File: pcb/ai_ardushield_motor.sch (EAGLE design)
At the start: 41 parts, among them IC1 PCA9685, IC2 TB6612FNG, IC3 TB6612FNG, J1 1X02ST, J10 1X04, J12 1X02ST, J2 1X03, J3 1X03, J4 1X06, J5 1X08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

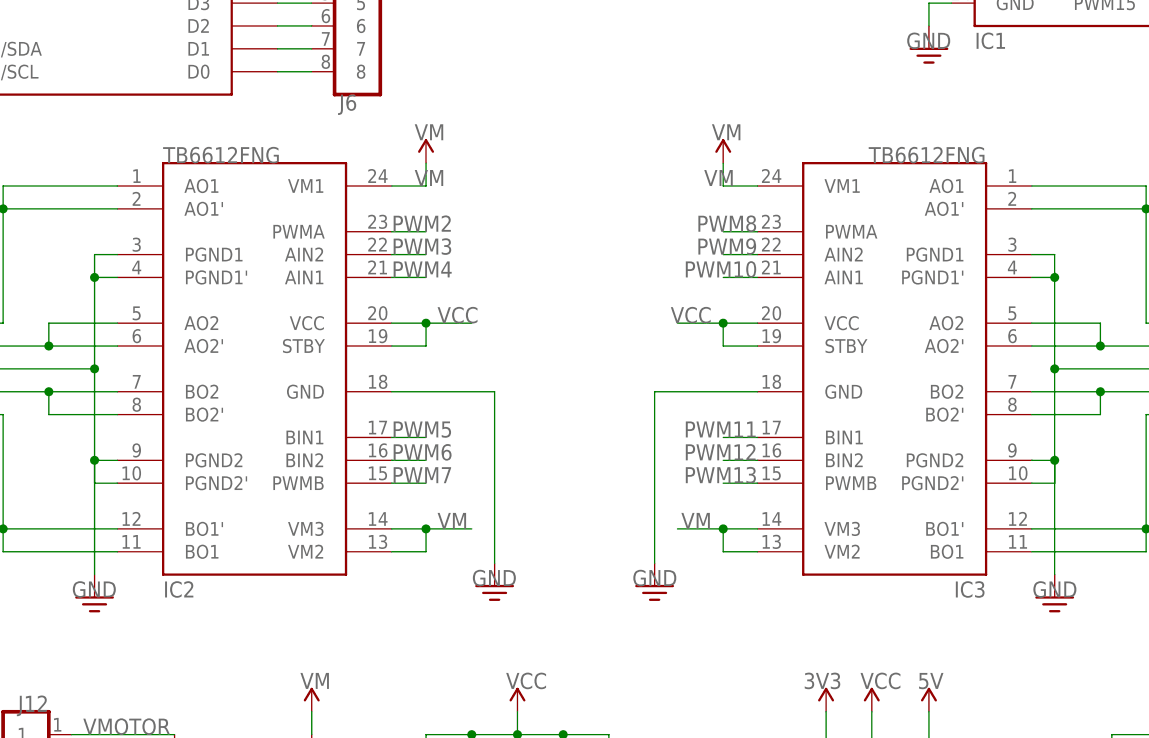
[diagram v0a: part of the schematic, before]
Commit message: Fixed a few minor warnings in the ERC.
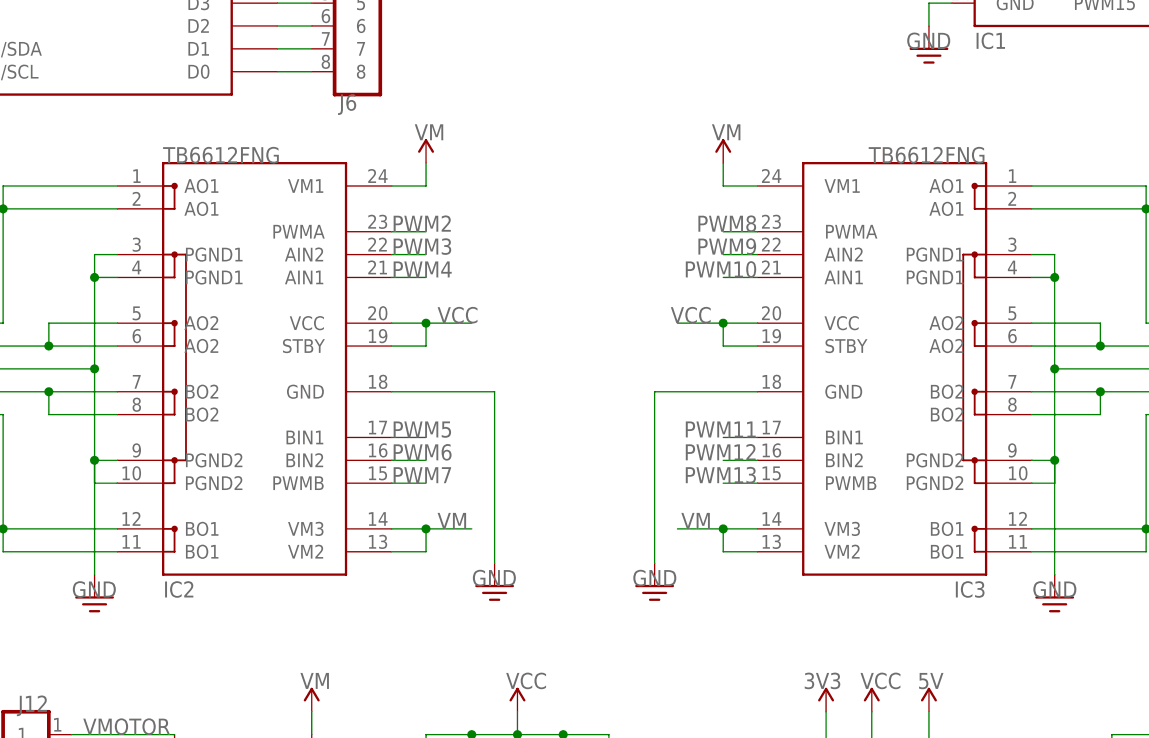
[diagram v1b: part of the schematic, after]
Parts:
- JS1, JS2, JS3, JS4, JS5: value (none) -> 1X02-SJNO
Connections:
- net GND: now also IC2.PGND1@1, IC2.PGND1@2, IC2.PGND2@1, IC2.PGND2@2, IC3.PGND1@1, IC3.PGND1@2, IC3.PGND2@1, IC3.PGND2@2; no longer IC2.PGND1, IC2.PGND1', IC2.PGND2, IC2.PGND2', IC3.PGND1, IC3.PGND1', IC3.PGND2, IC3.PGND2'
- net N$23: now also IC2.AO1@1, IC2.AO1@2; no longer IC2.AO1, IC2.AO1'
- net N$24: now also IC2.AO2@1, IC2.AO2@2; no longer IC2.AO2, IC2.AO2'
- net N$35: now also IC2.BO2@1, IC2.BO2@2; no longer IC2.BO2, IC2.BO2'
- net N$36: now also IC2.BO1@1, IC2.BO1@2; no longer IC2.BO1, IC2.BO1'
- net N$38: now also IC3.AO1@1, IC3.AO1@2; no longer IC3.AO1, IC3.AO1'
- net N$39: now also IC3.AO2@1, IC3.AO2@2; no longer IC3.AO2, IC3.AO2'
- net N$40: now also IC3.BO2@1, IC3.BO2@2; no longer IC3.BO2, IC3.BO2'
- net N$41: now also IC3.BO1@1, IC3.BO1@2; no longer IC3.BO1, IC3.BO1'
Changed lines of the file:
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@@
 <net name="N$23" class="1">
 <segment>
-<pinref part="IC2" gate="G$1" pin="AO1"/>
+<pinref part="IC2" gate="G$1" pin="AO1@1"/>
 <wire x1="77.47" y1="107.95" x2="64.77" y2="107.95" width="0.1524" layer="91"/>
 <wire x1="64.77" y1="107.95" x2="64.77" y2="105.41" width="0.1524" layer="91"/>
 <wire x1="64.77" y1="105.41" x2="64.77" y2="92.71" width="0.1524" layer="91"/>
 <wire x1="64.77" y1="92.71" x2="60.96" y2="92.71" width="0.1524" layer="91"/>
-<pinref part="IC2" gate="G$1" pin="AO1'"/>
+<pinref part="IC2" gate="G$1" pin="AO1@2"/>
 <wire x1="77.47" y1="105.41" x2="64.77" y2="105.41" width="0.1524" layer="91"/>
 <junction x="64.77" y="105.41"/>
@@
 <segment>
 <wire x1="77.47" y1="90.17" x2="69.85" y2="90.17" width="0.1524" layer="91"/>
-<pinref part="IC2" gate="G$1" pin="AO2"/>
+<pinref part="IC2" gate="G$1" pin="AO2@1"/>
 <wire x1="69.85" y1="90.17" x2="60.96" y2="90.17" width="0.1524" layer="91"/>
 <wire x1="77.47" y1="92.71" x2="69.85" y2="92.71" width="0.1524" layer="91"/>
 <wire x1="69.85" y1="92.71" x2="69.85" y2="90.17" width="0.1524" layer="91"/>
 <junction x="69.85" y="90.17"/>
-<pinref part="IC2" gate="G$1" pin="AO2'"/>
+<pinref part="IC2" gate="G$1" pin="AO2@2"/>
 <pinref part="J8" gate="G$1" pin="2"/>
 </segment>
@@
 <net name="N$35" class="1">
 <segment>
-<pinref part="IC2" gate="G$1" pin="BO2"/>
+<pinref part="IC2" gate="G$1" pin="BO2@1"/>
 <wire x1="60.96" y1="85.09" x2="69.85" y2="85.09" width="0.1524" layer="91"/>
-<pinref part="IC2" gate="G$1" pin="BO2'"/>
+<pinref part="IC2" gate="G$1" pin="BO2@2"/>
 <wire x1="69.85" y1="85.09" x2="77.47" y2="85.09" width="0.1524" layer="91"/>
 <wire x1="77.47" y1="82.55" x2="69.85" y2="82.55" width="0.1524" layer="91"/>
@@
 <wire x1="64.77" y1="82.55" x2="60.96" y2="82.55" width="0.1524" layer="91"/>
 <wire x1="64.77" y1="82.55" x2="64.77" y2="69.85" width="0.1524" layer="91"/>
-<pinref part="IC2" gate="G$1" pin="BO1"/>
+<pinref part="IC2" gate="G$1" pin="BO1@2"/>
 <wire x1="64.77" y1="69.85" x2="64.77" y2="67.31" width="0.1524" layer="91"/>
 <wire x1="64.77" y1="67.31" x2="77.47" y2="67.31" width="0.1524" layer="91"/>
-<pinref part="IC2" gate="G$1" pin="BO1'"/>
+<pinref part="IC2" gate="G$1" pin="BO1@1"/>
 <wire x1="77.47" y1="69.85" x2="64.77" y2="69.85" width="0.1524" layer="91"/>
 <pinref part="J8" gate="G$1" pin="5"/>
@@
 <net name="GND" class="1">
 <segment>
-<pinref part="IC2" gate="G$1" pin="PGND1"/>
+<pinref part="IC2" gate="G$1" pin="PGND1@1"/>
 <wire x1="74.93" y1="97.79" x2="74.93" y2="100.33" width="0.1524" layer="91"/>
 <wire x1="77.47" y1="100.33" x2="74.93" y2="100.33" width="0.1524" layer="91"/>
-<pinref part="IC2" gate="G$1" pin="PGND1'"/>
+<pinref part="IC2" gate="G$1" pin="PGND1@2"/>
 <wire x1="74.93" y1="97.79" x2="77.47" y2="97.79" width="0.1524" layer="91"/>
 <wire x1="74.93" y1="97.79" x2="74.93" y2="87.63" width="0.1524" layer="91"/>
@@
 <junction x="74.93" y="87.63"/>
 <junction x="74.93" y="97.79"/>
-<pinref part="IC2" gate="G$1" pin="PGND2'"/>
+<pinref part="IC2" gate="G$1" pin="PGND2@2"/>
 <wire x1="77.47" y1="74.93" x2="74.93" y2="74.93" width="0.1524" layer="91"/>
 <wire x1="74.93" y1="74.93" x2="74.93" y2="77.47" width="0.1524" layer="91"/>
-<pinref part="IC2" gate="G$1" pin="PGND2"/>
+<pinref part="IC2" gate="G$1" pin="PGND2@1"/>
 <wire x1="74.93" y1="77.47" x2="77.47" y2="77.47" width="0.1524" layer="91"/>
 <junction x="74.93" y="77.47"/>
@@
 </segment>
 <segment>
-<pinref part="IC3" gate="G$1" pin="PGND1"/>
+<pinref part="IC3" gate="G$1" pin="PGND1@1"/>
 <wire x1="181.61" y1="97.79" x2="181.61" y2="100.33" width="0.1524" layer="91"/>
 <wire x1="179.07" y1="100.33" x2="181.61" y2="100.33" width="0.1524" layer="91"/>
-<pinref part="IC3" gate="G$1" pin="PGND1'"/>
+<pinref part="IC3" gate="G$1" pin="PGND1@2"/>
 <wire x1="181.61" y1="97.79" x2="179.07" y2="97.79" width="0.1524" layer="91"/>
 <wire x1="181.61" y1="97.79" x2="181.61" y2="87.63" width="0.1524" layer="91"/>
@@
 <junction x="181.61" y="87.63"/>
 <junction x="181.61" y="97.79"/>
-<pinref part="IC3" gate="G$1" pin="PGND2'"/>
+<pinref part="IC3" gate="G$1" pin="PGND2@2"/>
 <wire x1="179.07" y1="74.93" x2="181.61" y2="74.93" width="0.1524" layer="91"/>
 <wire x1="181.61" y1="74.93" x2="181.61" y2="77.47" width="0.1524" layer="91"/>
-<pinref part="IC3" gate="G$1" pin="PGND2"/>
+<pinref part="IC3" gate="G$1" pin="PGND2@1"/>
 <wire x1="181.61" y1="77.47" x2="179.07" y2="77.47" width="0.1524" layer="91"/>
 <junction x="181.61" y="77.47"/>
@@
 <net name="N$38" class="1">
 <segment>
-<pinref part="IC3" gate="G$1" pin="AO1"/>
+<pinref part="IC3" gate="G$1" pin="AO1@1"/>
 <wire x1="179.07" y1="107.95" x2="191.77" y2="107.95" width="0.1524" layer="91"/>
 <wire x1="191.77" y1="107.95" x2="191.77" y2="105.41" width="0.1524" layer="91"/>
 <wire x1="191.77" y1="105.41" x2="191.77" y2="92.71" width="0.1524" layer="91"/>
 <wire x1="191.77" y1="92.71" x2="195.58" y2="92.71" width="0.1524" layer="91"/>
-<pinref part="IC3" gate="G$1" pin="AO1'"/>
+<pinref part="IC3" gate="G$1" pin="AO1@2"/>
 <wire x1="179.07" y1="105.41" x2="191.77" y2="105.41" width="0.1524" layer="91"/>
 <junction x="191.77" y="105.41"/>
@@
 <segment>
 <wire x1="179.07" y1="90.17" x2="186.69" y2="90.17" width="0.1524" layer="91"/>
-<pinref part="IC3" gate="G$1" pin="AO2"/>
+<pinref part="IC3" gate="G$1" pin="AO2@1"/>
 <wire x1="186.69" y1="90.17" x2="195.58" y2="90.17" width="0.1524" layer="91"/>
 <wire x1="179.07" y1="92.71" x2="186.69" y2="92.71" width="0.1524" layer="91"/>
 <wire x1="186.69" y1="92.71" x2="186.69" y2="90.17" width="0.1524" layer="91"/>
 <junction x="186.69" y="90.17"/>
-<pinref part="IC3" gate="G$1" pin="AO2'"/>
+<pinref part="IC3" gate="G$1" pin="AO2@2"/>
 <pinref part="J9" gate="G$1" pin="2"/>
 </segment>
@@
 <net name="N$40" class="1">
 <segment>
-<pinref part="IC3" gate="G$1" pin="BO2"/>
+<pinref part="IC3" gate="G$1" pin="BO2@1"/>
 <wire x1="195.58" y1="85.09" x2="186.69" y2="85.09" width="0.1524" layer="91"/>
-<pinref part="IC3" gate="G$1" pin="BO2'"/>
+<pinref part="IC3" gate="G$1" pin="BO2@2"/>
 <wire x1="186.69" y1="85.09" x2="179.07" y2="85.09" width="0.1524" layer="91"/>
 <wire x1="179.07" y1="82.55" x2="186.69" y2="82.55" width="0.1524" layer="91"/>
@@
 <wire x1="191.77" y1="82.55" x2="195.58" y2="82.55" width="0.1524" layer="91"/>
 <wire x1="191.77" y1="82.55" x2="191.77" y2="69.85" width="0.1524" layer="91"/>
-<pinref part="IC3" gate="G$1" pin="BO1"/>
+<pinref part="IC3" gate="G$1" pin="BO1@2"/>
 <wire x1="191.77" y1="69.85" x2="191.77" y2="67.31" width="0.1524" layer="91"/>
 <wire x1="191.77" y1="67.31" x2="179.07" y2="67.31" width="0.1524" layer="91"/>
-<pinref part="IC3" gate="G$1" pin="BO1'"/>
+<pinref part="IC3" gate="G$1" pin="BO1@1"/>
 <wire x1="179.07" y1="69.85" x2="191.77" y2="69.85" width="0.1524" layer="91"/>
 <pinref part="J9" gate="G$1" pin="5"/>
@@
 <junction x="111.76" y="69.85"/>
 <label x="113.03" y="69.85" size="1.778" layer="95"/>
-<label x="110.49" y="107.95" size="1.778" layer="95"/>
 </segment>
 <segment>
@@
 <junction x="144.78" y="69.85"/>
 <label x="143.51" y="69.85" size="1.778" layer="95" rot="MR0"/>
-<label x="146.05" y="107.95" size="1.778" layer="95" rot="MR0"/>
-</segment>
-<segment>
+</segment>
+<segment>

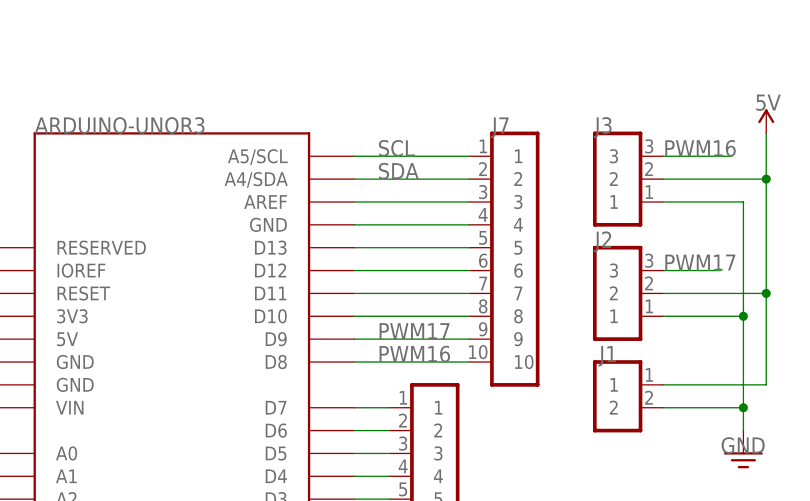
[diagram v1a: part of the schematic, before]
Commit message: changed the pcb dimension width.
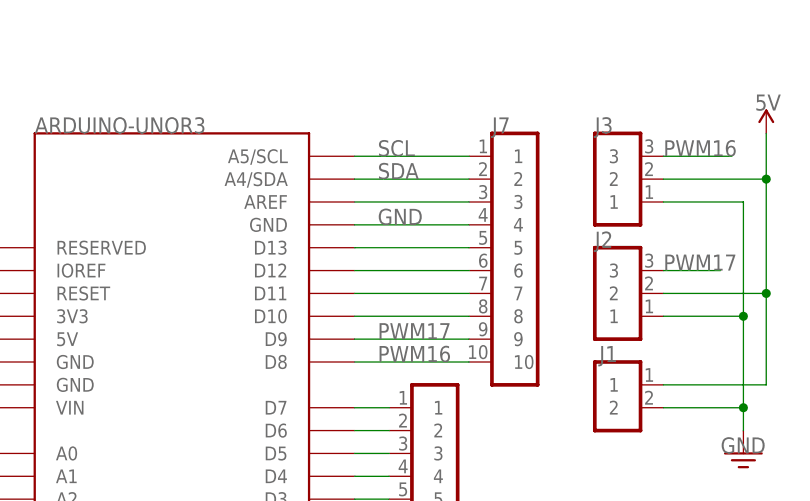
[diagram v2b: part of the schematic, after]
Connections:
- removed net N$28: J7.4, U1.GND@3
- net GND: now also J7.4, U1.GND@3
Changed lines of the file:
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@@
 <attribute name="NAME" x="104.14" y="118.11" size="1.778" layer="95" rot="R180"/>
 </instance>
-<instance part="IC2" gate="G$1" x="92.71" y="87.63"/>
+<instance part="IC2" gate="G$1" x="92.71" y="87.63" smashed="yes">
+<attribute name="NAME" x="82.55" y="62.23" size="1.778" layer="95"/>
+</instance>
 <instance part="IC1" gate="G$1" x="182.88" y="151.13"/>
 <instance part="GND1" gate="GND" x="74.93" y="62.23"/>
@@
 </segment>
 </net>
-<net name="N$28" class="0">
-<segment>
-<pinref part="U1" gate="G$1" pin="GND@3"/>
-<pinref part="J7" gate="M10X1" pin="4"/>
-<wire x1="107.95" y1="158.75" x2="95.25" y2="158.75" width="0.1524" layer="91"/>
-</segment>
-</net>
 <net name="N$29" class="0">
 <segment>
@@
 <wire x1="203.2" y1="31.75" x2="203.2" y2="34.29" width="0.1524" layer="91"/>
 </segment>
-</net>
+<segment>
+<pinref part="U1" gate="G$1" pin="GND@3"/>
+<pinref part="J7" gate="M10X1" pin="4"/>
+<wire x1="107.95" y1="158.75" x2="95.25" y2="158.75" width="0.1524" layer="91"/>
+<label x="97.79" y="158.75" size="1.778" layer="95"/>
+</segment>
+</net>

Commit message: New version including detailed BOM
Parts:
- added J11, J13, J14, J15, J16, J17, J18, J19, J20, J21, J22: 1X06-PROTO, Ai_Connectors:1X06-PROTO
- added U$14: AI-LOGOL, Ai_Miscellany:AI-LOGOL
- C1, C2, C3: device Ai_Passives:CAP_POLC -> Ai_Passives:CAP-POLPANASONIC-C
- C4, C5, C6, C7, C8: device Ai_Passives:CAP -> Ai_Passives:CAP0603
- J10: value 1X04 -> 1X02ST; device Ai_Connectors:1X04 -> Ai_Connectors:1X02ST
- J12: value 1X02ST -> 1X06-PROTO; device Ai_Connectors:1X02ST -> Ai_Connectors:1X06-PROTO
- J2: value 1X03 -> 2X03; device Ai_Connectors:1X03 -> Ai_Connectors:2X03
- J3: value 1X03 -> 1X06; device Ai_Connectors:1X03 -> Ai_Connectors:1X06
- J4: value 1X06 -> 1X08; device Ai_Connectors:1X06 -> Ai_Connectors:1X08
- J6: value 1X08 -> 1X10; device Ai_Connectors:1X08 -> Ai_Connectors:1X10
- J7: value 1X10 -> 1X05ST; device Ai_Connectors:1X10 -> Ai_Connectors:1X05ST
- J9: value 1X05ST -> 1X04; device Ai_Connectors:1X05ST -> Ai_Connectors:1X04
- R1: value 1k -> 1K; device Ai_Passives:RES -> Ai_Passives:RES0603
- R2, R3, R4, R5, R6, R7, R8: device Ai_Passives:RES -> Ai_Passives:RES0603
- SW1: value SW-SPST -> SW-SPSTSMD06X06; device Ai_Electromechanical:SW-SPST -> Ai_Electromechanical:SW-SPSTSMD06X06
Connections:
- net 3V3: now also J4.5; no longer J5.5
- net 5V: now also J2.3, J2.4, J4.4; no longer J2.2, J3.2, J5.4
- net GND: now also J10.2, J2.2, J4.2, J4.3, J6.4, J7.3; no longer J12.2, J3.1, J5.2, J5.3, J7.4, J9.3
- net N$1: now also J5.1; no longer J6.1
- net N$15: now also J4.7; no longer J5.7
- net N$16: now also J4.8; no longer J5.8
- net N$17: now also J5.3; no longer J6.3
- net N$18: now also J5.4; no longer J6.4
- net N$19: now also J5.5; no longer J6.5
- net N$2: now also J5.2; no longer J6.2
- net N$20: now also J5.6; no longer J6.6
- net N$21: now also J5.7; no longer J6.7
- net N$22: now also J5.8; no longer J6.8
- net N$23: now also J7.1; no longer J8.1
- net N$24: now also J7.2; no longer J8.2
- net N$27: now also J6.3; no longer J7.3
- net N$29: now also J6.5; no longer J7.5
- net N$30: now also J6.6; no longer J7.6
- net N$31: now also J6.7; no longer J7.7
- net N$32: now also J6.8; no longer J7.8
- net N$35: now also J7.4; no longer J8.4
- net N$36: now also J7.5; no longer J8.5
- net N$38: now also J8.1; no longer J9.1
- net N$39: now also J8.2; no longer J9.2
- net N$40: now also J8.4; no longer J9.4
- net N$41: now also J8.5; no longer J9.5
- net N$5: now also J3.3; no longer J4.3
- net N$6: now also J3.4; no longer J4.4
- net N$7: now also J3.5; no longer J4.5
- net N$8: now also J3.6; no longer J4.6
- net PWM0: now also J9.1; no longer J10.1
- net PWM1: now also J9.2; no longer J10.2
- net PWM14: now also J9.3; no longer J10.3
- net PWM15: now also J9.4; no longer J10.4
- net PWM16: now also J2.6, J6.10; no longer J3.3, J7.10
- net PWM17: now also J2.5, J6.9; no longer J2.3, J7.9
- net RESET: now also J4.6; no longer J5.6
- net SCL: now also J3.1, J6.1; no longer J4.1, J7.1
- net SDA: now also J3.2, J6.2; no longer J4.2, J7.2
- net VIN: now also J4.1; no longer J5.1
- net VMOTOR: now also J10.1; no longer J12.1
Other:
- note added: "PADS FOR PROTOTYPING REGION"
- note added: "VMOTOR"
- moved on the sheet: IC2, IC3, J1, JP1, LED1, Q1, R1, SW1
